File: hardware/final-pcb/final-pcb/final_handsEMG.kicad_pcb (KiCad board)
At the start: 2 copper layers, 192 parts, among them J1 Conn_02x13_Odd_Even, U1 ADS1299CPAG, U2 STM32L496ZGT6, U3 FT231XQ-R, U6 TPS60403DBVT, U8 TPS72325DBVT, U9 TPS73225DBVT

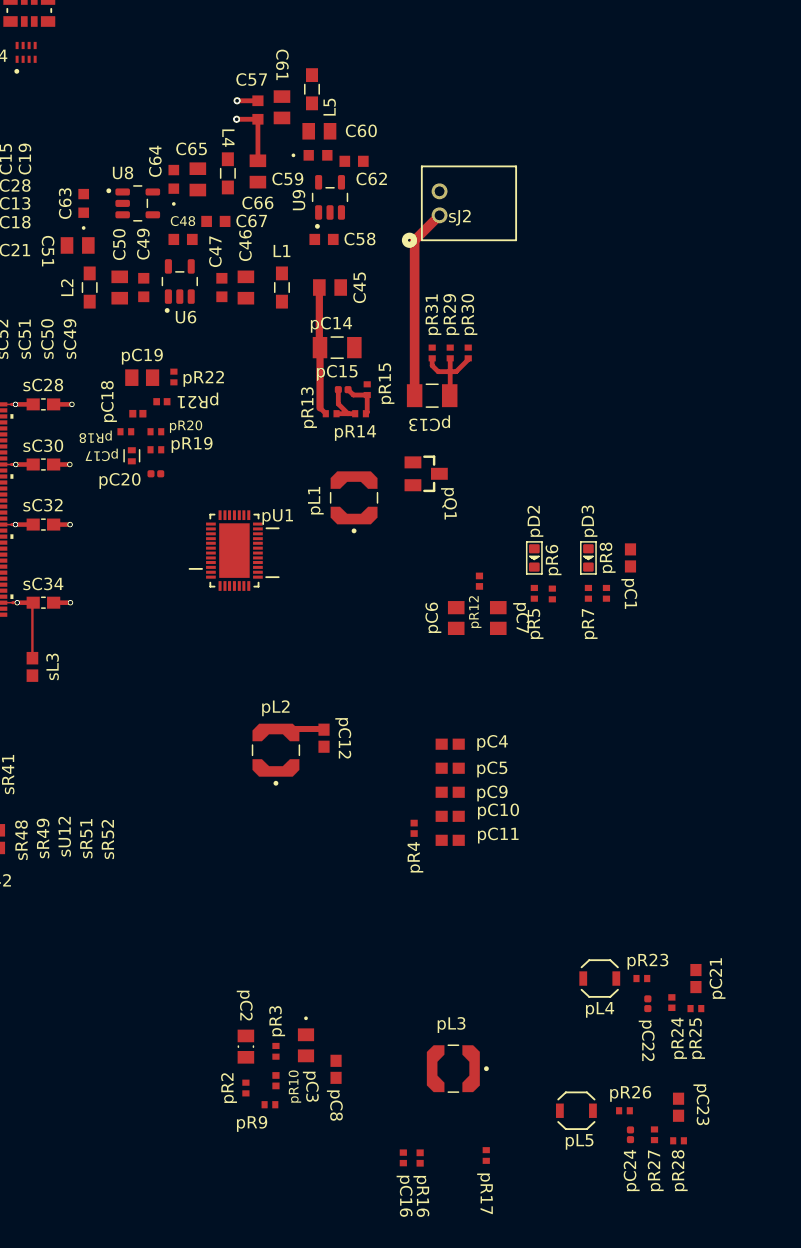
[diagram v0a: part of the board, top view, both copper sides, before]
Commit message: Power routed, not clean but in
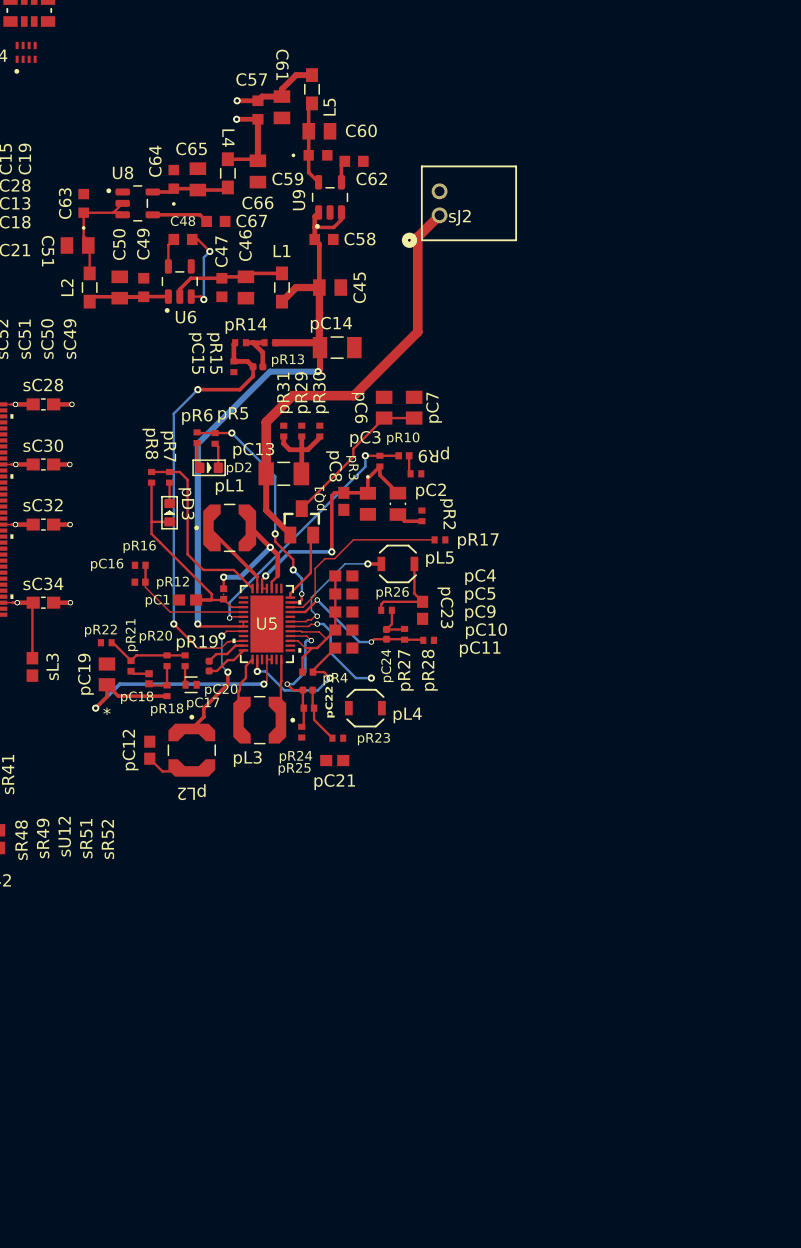
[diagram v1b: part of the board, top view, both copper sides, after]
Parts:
- removed pU1: LTC3586EUFE-3-PBF, 03PowerFOOTPRINTS:LTC3586EUFE
- added U5: LTC3586EUFE-3-PBF, footprints:QFN-38_UFE_LIT, F.Cu at (138.7, 99.5)
- pR34, pR35: value 1K -> 10K
- moved pC16 53.9 mm to (128.2, 94.6), turned to 180 degrees
- moved pR9 53.9 mm to (151.1, 87.0), turned to 180 degrees
- moved pR16 53.3 mm to (128.2, 96.0), turned to 180 degrees
- moved pR10 53.1 mm to (150.1, 85.5), turned to 180 degrees
- moved pR17 51.4 mm to (153.1, 92.5), turned to 0 degrees
- moved pR3 49.9 mm to (148.1, 85.9), turned to 90 degrees
- moved pR2 49.8 mm to (151.6, 90.5), turned to 90 degrees
- moved pL5 47.9 mm to (149.6, 94.5)
- moved pC8 47.3 mm to (145.1, 89.3)
- moved pC2 46.9 mm to (149.6, 89.5)
- moved pR27 46.5 mm to (150.2, 100.4)
- moved pR28 46.5 mm to (152.2, 100.9)
- moved pC23 46.5 mm to (151.7, 98.4)
- moved pC24 46.3 mm to (148.7, 100.4)
- moved pR26 46.1 mm to (148.7, 98.4)
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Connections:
- U1 pad 35: /PWDN -> PC4
- U1 pad 36: /RESET -> PC5
- U1 pad 38: START -> PB0
- U1 pad 39: /CS -> PA4
- U1 pad 40: SCLK -> PA1
- U1 pad 47: /DRDY -> PA5
- U2 pad 111: unconnected-(U2-PC10-Pad111) -> MODE
- U2 pad 112: unconnected-(U2-PC11-Pad112) -> ILIM1
- U2 pad 113: unconnected-(U2-PC12-Pad113) -> ILIM0
- U2 pad 114: unconnected-(U2-PD0-Pad114) -> *FAULT
- U2 pad 115: unconnected-(U2-PD1-Pad115) -> EN1
- U2 pad 116: unconnected-(U2-PD2-Pad116) -> EN2
- U2 pad 117: unconnected-(U2-PD3-Pad117) -> EN3
- U2 pad 118: unconnected-(U2-PD4-Pad118) -> EN4
- U2 pad 119: unconnected-(U2-PD5-Pad119) -> PD5
- U2 pad 122: unconnected-(U2-PD6-Pad122) -> PD6
- U2 pad 41: unconnected-(U2-PA5-Pad41) -> PA5
- U2 pad 42: PA6 -> DOUT
- U2 pad 43: PA7 -> DIN
- U2 pad 44: unconnected-(U2-PC4-Pad44) -> PC4
- U2 pad 45: unconnected-(U2-PC5-Pad45) -> PC5
- U2 pad 46: unconnected-(U2-PB0-Pad46) -> PB0
- dR6 pad 1: RXD -> PD5
- dR6 pad 2: Net-(U3-RXD) -> Net-(U4-RXD)
- dR7 pad 1: TXD -> PD6
- dR7 pad 2: Net-(U3-TXD) -> Net-(U4-TXD)
- pR34 pad 1: Net-(pJP7-Pad1) -> EN3
- pR35 pad 1: Net-(pJP8-Pad1) -> EN4
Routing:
- net 5VCC: track 10.7 -> 65.6 mm, vias 0 -> 2
- net PVIN3: track 4.02 -> 43.6 mm, vias 0 -> 2
- net FB4: track 3.38 -> 36.5 mm, vias 0 -> 2
- net AVOUT3: track 69.0 -> 94.1 mm, vias 19 -> 21
- net NTC: track 0.00 -> 22.1 mm, vias 0 -> 2
- net AVBUS: track 11.6 -> 32.9 mm, vias 0 -> 2
- net BAT: track 15.9 -> 36.8 mm
- net *CHRG: track 0.00 -> 20.2 mm, vias 0 -> 4
- net LDO3V3: track 0.00 -> 19.7 mm
- net -5VCC: track 0.00 -> 18.4 mm
- net *FAULT: track 0.00 -> 16.0 mm
- net PROG: track 0.00 -> 15.6 mm
- net unconnected-(U3-CTS#-Pad6): track 0.00 -> 13.2 mm, vias 0 -> 2
- net Net-(U3-RXD): track 13.2 -> 0.00 mm, vias 2 -> 0
- net FB1: track 0.00 -> 13.1 mm, vias 0 -> 2
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
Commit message: finalpcb is not final yet (4.12.25)
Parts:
- removed U5: LTC3586EUFE-3-PBF, footprints:QFN-38_UFE_LIT
- removed pC26, pC27: 0.1uF, 03PowerFOOTPRINTS:C1005X5R1C104K
- removed pJP2, pJP3, pJP4, pJP5, pJP6, pJP7, pJP8: TMM-103-02-L-S, 03PowerFOOTPRINTS:SAMTEC-TMM-103-02-X-S
- removed pR32, pR33: 1K, 03PowerFOOTPRINTS:CRCW04021K00JNED
- added U3: LTC3586EUFE-3-PBF, 03PowerFOOTPRINTS:LTC3586EUFE, F.Cu at (145.7, 99.9)
- moved pR34 54.4 mm to (177.9, 47.7)
- moved pR35 54.4 mm to (177.9, 49.9)
- moved pC29 47.1 mm to (177.9, 45.5)
- moved pC28 41.4 mm to (177.9, 43.4)
- moved pD3 30.2 mm to (156.7, 74.8), turned to -90 degrees
- moved pR9 28.2 mm to (131.8, 107.5), turned to 0 degrees
- moved pR10 27.6 mm to (131.8, 106.1)
- moved pC19 27.2 mm to (151.2, 112.4), turned to -90 degrees
- moved C63 26.0 mm to (147.0, 53.5), turned to 0 degrees
- moved pR15 25.5 mm to (140.7, 103.1), turned to 0 degrees
- moved C51 24.6 mm to (147.5, 70.1), turned to 90 degrees
- moved pR3 24.5 mm to (131.8, 104.2), turned to 180 degrees
- moved pR14 23.7 mm to (140.2, 99.5), turned to 180 degrees
- moved pC15 23.5 mm to (140.7, 101.4), turned to 0 degrees
- moved U8 23.1 mm to (145.3, 49.2), turned to 90 degrees
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- renumbered U3 to U4
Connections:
- U2 pad 107: GND -> DGND
- U2 pad 120: GND -> DGND
- U2 pad 130: GND -> DGND
- U2 pad 143: GND -> DGND
- U2 pad 16: GND -> DGND
- U2 pad 30: GNDA -> DGND
- U2 pad 31: GNDA -> DGND
- U2 pad 38: GND -> DGND
- U2 pad 51: GND -> DGND
- U2 pad 6: VBAT -> AVOUT3
- U2 pad 61: GND -> DGND
- U2 pad 71: GND -> DGND
- U2 pad 83: GND -> DGND
- U2 pad 94: GND -> DGND
- U4 pad 1: Net-(U3-RXD) -> Net-(U4-RXD)
- U4 pad 12: AVBUS -> AVOUT3
- U4 pad 13: GND -> DGND
- U4 pad 17: Net-(U3-TXD) -> Net-(U4-TXD)
- U4 pad 18: DTR# -> unconnected-(U4-DTR#-Pad18)
- U4 pad 20: 3V3OUT -> AVOUT3
- U4 pad 21: GND -> DGND
- U4 pad 3: GND -> DGND
- dC1 pad 2: GND -> DGND
- dC2 pad 2: GND -> DGND
- dC3 pad 2: GND -> DGND
- dD3 pad 2: GND -> DGND
- pC1 pad 2: GND -> DGND
- pC10 pad 2: GND -> DGND
- pC11 pad 2: GND -> DGND
- pC12 pad 2: GND -> DGND
- pC14 pad 2: GND -> DGND
- pC16 pad 2: GND -> DGND
- pC19 pad 2: GND -> DGND
- pC21 pad 1: GND -> DGND
- pC23 pad 1: GND -> DGND
- pC28 pad 2: GND -> DGND
- pC29 pad 2: GND -> DGND
- pC3 pad 2: GND -> DGND
- pC4 pad 2: GND -> DGND
- pC5 pad 2: GND -> DGND
- pC6 pad 2: GND -> DGND
- pC7 pad 2: GND -> DGND
- pC8 pad 2: GND -> DGND
- pC9 pad 2: GND -> DGND
- pR15 pad 1: GND -> DGND
- pR16 pad 2: GND -> DGND
- pR17 pad 2: GND -> DGND
- pR2 pad 2: GND -> DGND
- pR22 pad 2: GND -> DGND
- pR25 pad 2: GND -> DGND
- pR28 pad 2: GND -> DGND
- pR29 pad 1: GND -> DGND
- pR30 pad 1: GND -> DGND
- pR31 pad 1: GND -> DGND
- pR9 pad 1: GND -> DGND
- sC28 pad 2: GND -> DGND
- sC29 pad 2: GND -> DGND
- sC30 pad 2: GND -> DGND
- sC31 pad 2: GND -> DGND
- sC32 pad 2: GND -> DGND
- sC33 pad 2: GND -> DGND
- sC34 pad 2: GND -> DGND
- sC42 pad +: (no net) -> AVBUS
- sC42 pad -: (no net) -> DGND
- sC49 pad 2: GND -> DGND
- sC50 pad 2: GND -> DGND
- sC51 pad 2: GND -> DGND
- sC52 pad 2: GND -> DGND
- sC53 pad 2: GND -> DGND
- sC54 pad 2: GND -> DGND
- sC57 pad 2: GNDA -> DGND
- sC58 pad 2: GNDA -> DGND
- sC60 pad 2: GND -> DGND
- sC61 pad 2: GND -> DGND
- sCN14 pad 5: GND -> DGND
- sD10 pad 2: GND -> DGND
- sD6 pad 2: GND -> DGND
- sJ2 pad 2: GND -> DGND
- sJ3 pad 5: GND -> DGND
- sJ3 pad 7: GND -> DGND
- sLD7 pad +: (no net) -> Net-(sLD7-A)
- sLD7 pad -: (no net) -> Net-(sLD7-K)
- sLD8 pad +: (no net) -> Net-(sLD8-A)
- sLD8 pad -: (no net) -> Net-(sLD8-K)
- sR38 pad 2: GND -> DGND
- sR48 pad 1: GND -> DGND
- sR52 pad 2: GND -> DGND
- sT2 pad 2: GND -> DGND
- sU12 pad 2: GND -> DGND
- sU13 pad 2: GND -> DGND
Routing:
- net AVSS: track 7.78 -> 151.8 mm, vias 1 -> 20
- net AVDD: track 13.4 -> 149.9 mm, vias 3 -> 17
- net DGND: track 0.00 -> 129.9 mm, vias 0 -> 73
- net AVBUS: track 32.9 -> 122.8 mm, vias 2 -> 6
- net GNDA: track 2.88 -> 82.3 mm, vias 2 -> 52
- net ILIM1: track 0.00 -> 78.9 mm, vias 0 -> 2
- net ILIM0: track 0.00 -> 78.0 mm, vias 0 -> 2
- net EN2: track 0.00 -> 76.8 mm, vias 0 -> 3
- net EN1: track 0.00 -> 74.1 mm, vias 0 -> 2
- net EN4: track 0.00 -> 67.4 mm, vias 0 -> 2
- net MODE: track 0.00 -> 67.0 mm, vias 0 -> 2
- net EN3: track 0.00 -> 66.7 mm, vias 0 -> 2
- net *FAULT: track 16.0 -> 77.4 mm, vias 0 -> 3
- net PA10: track 0.00 -> 52.5 mm, vias 0 -> 2
- net PA5: track 0.00 -> 46.9 mm, vias 0 -> 2
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- added copper zone on In1.Cu, net AVDD
- added copper zone on In1.Cu, net AVOUT3
- added copper zone on B.Cu, net DGND
- added copper zone on F.Cu, net DGND
- added copper zone on In2.Cu, net DGND
- added copper zone on B.Cu, net GNDA
- added copper zone on F.Cu, net GNDA
- added copper zone on In2.Cu, net GNDA
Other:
- board outline added: 85.2 x 104 mm
- copper layers 2 -> 4

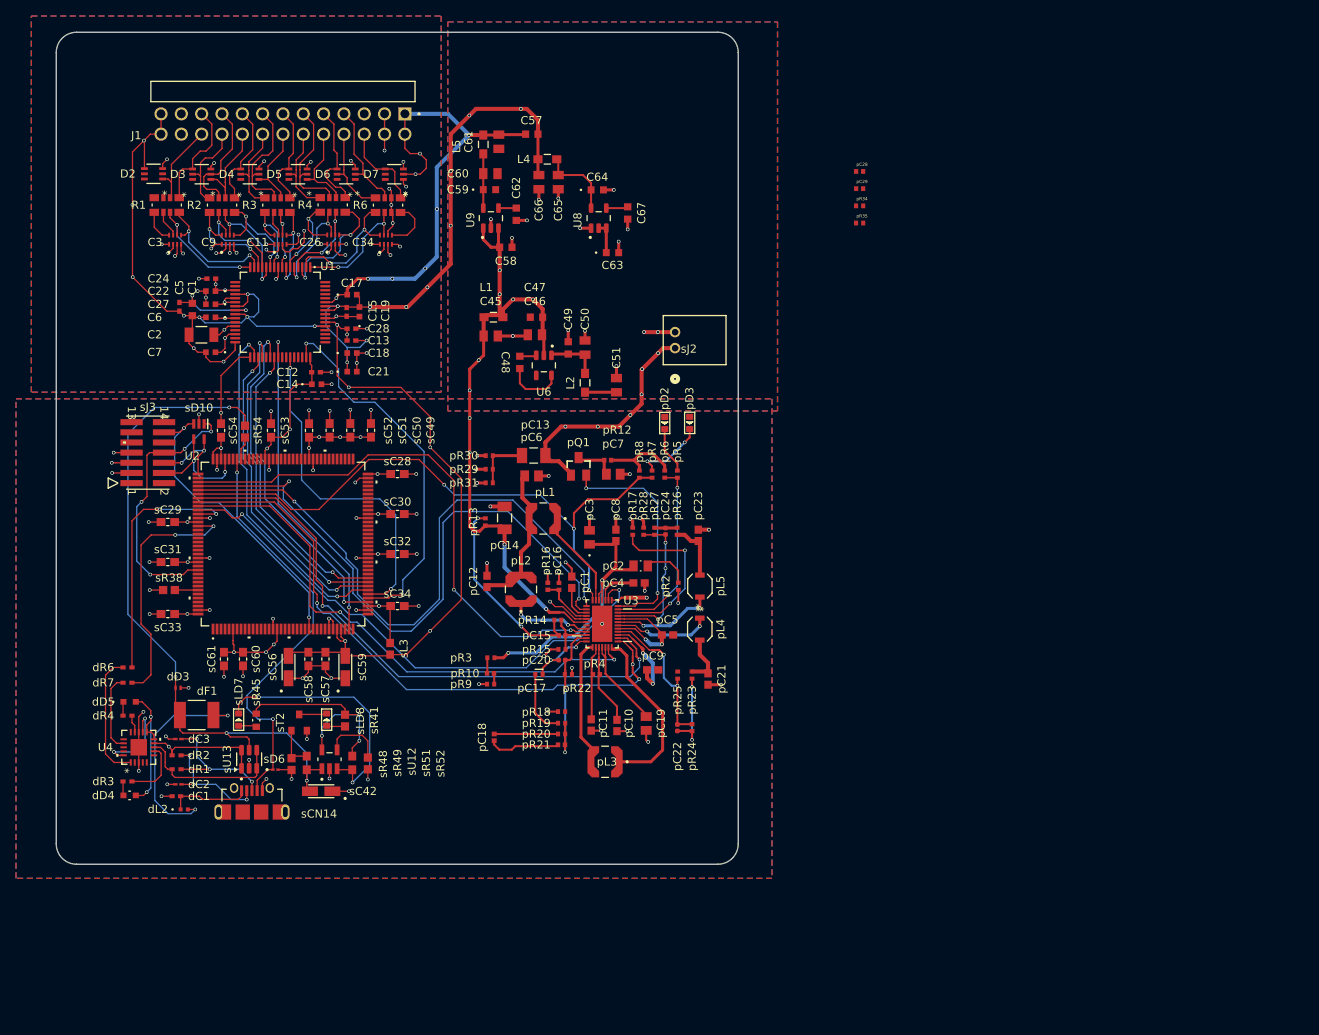
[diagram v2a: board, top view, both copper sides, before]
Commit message: traces got fucked up so i rerouted pmic (4.13.25)
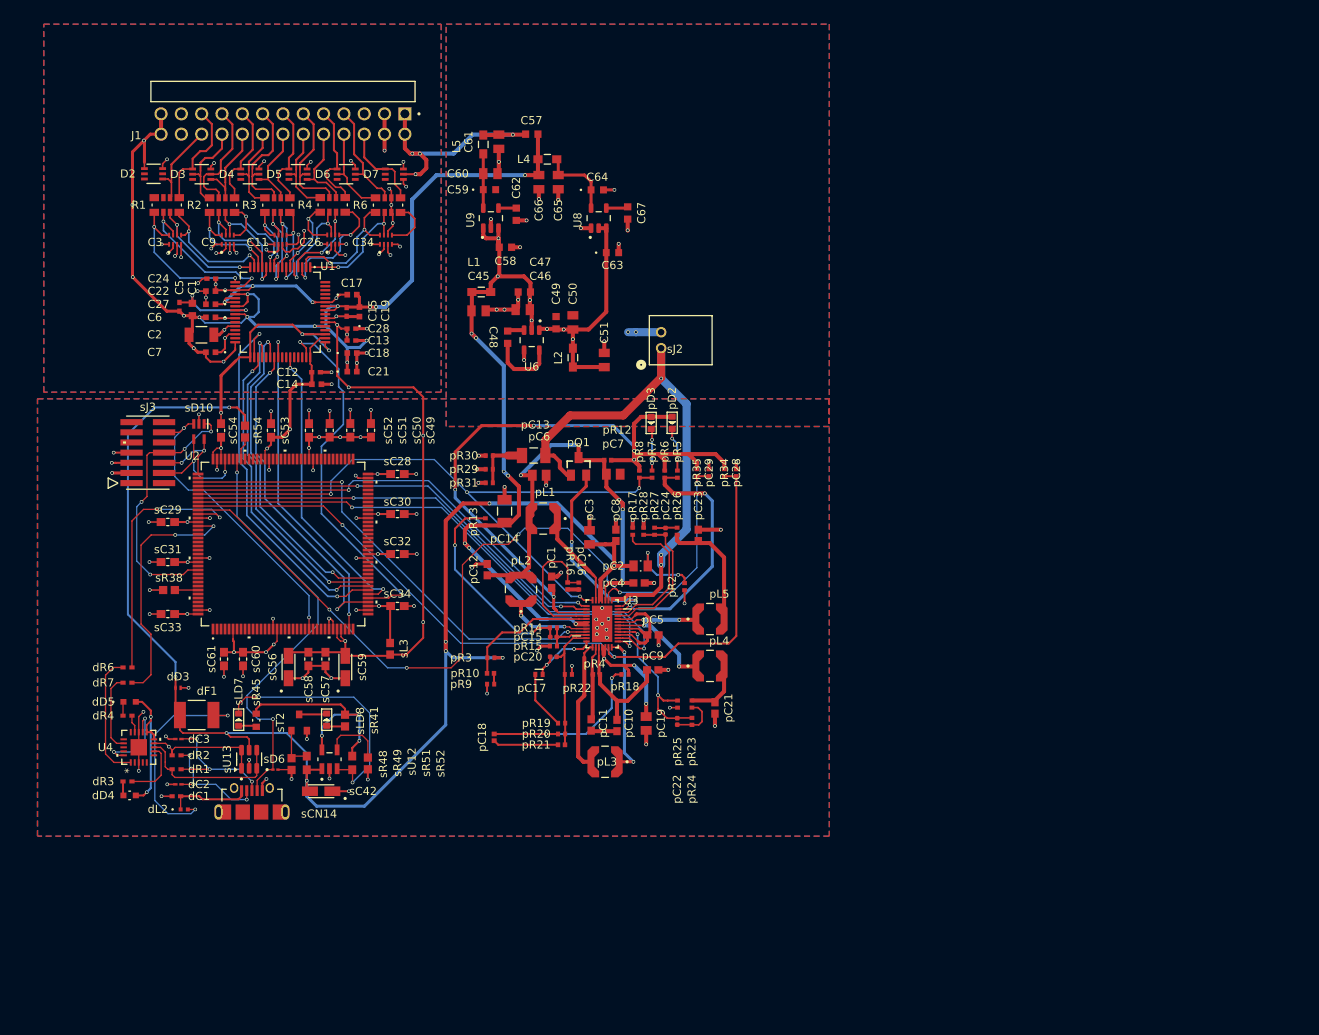
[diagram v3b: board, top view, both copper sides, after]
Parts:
- pL4, pL5: footprint 03PowerFOOTPRINTS:IND_3010_TDK -> LPS4018_472MRC:IND_LPS4018-472MRC
- moved pC28 40.7 mm to (162.5, 81.1), turned to 90 degrees
- moved pC29 40.2 mm to (159.1, 81.1), turned to 90 degrees
- moved pR34 37.4 mm to (161.0, 81.1), turned to 90 degrees
- moved pR35 37.3 mm to (157.6, 81.1), turned to 90 degrees
- moved pR18 9.19 mm to (148.6, 106.3)
- moved pD3 4.81 mm to (151.9, 74.8)
- moved pL4 4.77 mm to (159.2, 105.2), turned to 0 degrees
- moved pL5 4.31 mm to (159.2, 99.4), turned to 0 degrees
- moved pC21 3.72 mm to (159.8, 110.5)
- moved pR23 3.62 mm to (157.0, 110.0)
- moved pR25 3.62 mm to (155.2, 110.0), turned to -90 degrees
- moved C51 3.50 mm to (146.0, 67.0)
- moved C47 3.50 mm to (136.0, 58.5)
- moved C49 3.50 mm to (140.0, 62.3)
- moved L1 3.50 mm to (130.6, 58.5)
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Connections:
- C45 pad 2: GNDA -> DGND
- C46 pad 2: GNDA -> DGND
- C47 pad 2: GNDA -> DGND
- C49 pad 2: GNDA -> DGND
- C50 pad 2: GNDA -> DGND
- C51 pad 2: GNDA -> DGND
- C58 pad 2: GNDA -> DGND
- C59 pad 2: GNDA -> DGND
- C60 pad 2: GNDA -> DGND
- C61 pad 2: GNDA -> DGND
- C62 pad 2: GNDA -> DGND
- C63 pad 2: GNDA -> DGND
- C64 pad 2: GNDA -> DGND
- C65 pad 2: GNDA -> DGND
- C66 pad 2: GNDA -> DGND
- C67 pad 2: GNDA -> DGND
- U6 pad 4: GNDA -> DGND
- U8 pad 1: GNDA -> DGND
- U9 pad 2: GNDA -> DGND
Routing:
- net LDO3V3: track 13.5 -> 88.0 mm, vias 0 -> 5
- net AVBUS: track 122.8 -> 184.8 mm, vias 6 -> 9
- net DGND: track 129.9 -> 174.7 mm, vias 73 -> 98
- net EN4: track 67.4 -> 106.3 mm, vias 2 -> 5
- net BAT: track 34.1 -> 68.3 mm, vias 7 -> 3
- net EN3: track 66.7 -> 98.6 mm
- net ILIM1: track 78.9 -> 53.6 mm
- net PVIN3: track 60.3 -> 81.3 mm, vias 4 -> 5
- net ILIM0: track 78.0 -> 57.0 mm
- net GNDA: track 82.3 -> 63.6 mm, vias 52 -> 39
- net SRB2: track 3.35 -> 20.5 mm, vias 0 -> 2
- net SRB1: track 4.13 -> 19.3 mm, vias 0 -> 2
- net -5VCC: track 14.6 -> 29.4 mm, vias 0 -> 3
- net AVDD: track 149.9 -> 135.8 mm, vias 17 -> 16
- net Net-(pC18-Pad1): track 9.21 -> 22.7 mm, vias 1 -> 2
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- added copper zone on In1.Cu, net AVSS
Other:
- board outline removed

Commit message: basically done, everyone please verify if possible (4.16.25)
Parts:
- added C16: 1nF, CC0402KRX7R7BB102:YAG_CC0402_YAG, F.Cu at (114.4, 57.4)
- added G***: LOGO, LOGO, F.Cu at (156.9, 49.1)
- added R5: 1M, RC0402JR-071ML:RC0402N_YAG, F.Cu at (114.4, 56.0)
- added REF**: MountingHole_2.1mm, MountingHole:MountingHole_2.1mm, F.Cu at (82.5, 34.6)
- added REF**: MountingHole_2.1mm, MountingHole:MountingHole_2.1mm, F.Cu at (163.3, 123.9)
- added REF**: MountingHole_2.1mm, MountingHole:MountingHole_2.1mm, F.Cu at (163.3, 34.6)
- added REF**: MountingHole_2.1mm, MountingHole:MountingHole_2.1mm, F.Cu at (82.5, 123.9)
- added TP1: RAW, 5000:KEYSTONE_5000, F.Cu at (161.6, 73.6)
- added TP2: LDO3V3, 5000:KEYSTONE_5000, F.Cu at (137.2, 72.0)
- added TP4: +3V3, 5000:KEYSTONE_5000, F.Cu at (146.0, 121.7)
- added TP5: -5V, 5001:KEYSTONE_5001, F.Cu at (150.8, 58.5)
- added TP6: +5V, 5001:KEYSTONE_5001, F.Cu at (129.4, 67.6)
- added TP7: +2V5, 5001:KEYSTONE_5001, F.Cu at (129.6, 35.8)
- added TP8: -2V5, 5001:KEYSTONE_5001, F.Cu at (145.2, 38.8)
- moved BAT 4.65 mm to (157.8, 65.5)
- moved SWD 2.47 mm to (86.5, 78.5)
- renumbered sJ2 to BAT, sJ3 to SWD
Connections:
- C3 pad 7: SRB2 -> _SRB2
- C3 pad 8: SRB1 -> _SRB1
- R1 pad 5: SRB1 -> _SRB1
- R1 pad 6: SRB2 -> _SRB2
- U1 pad 17: SRB1 -> _SRB1
- U1 pad 18: SRB2 -> _SRB2
- U1 pad 63: BIASOUT -> BIASIN
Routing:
- net _SRB2: track 0.00 -> 20.5 mm, vias 0 -> 2
- net _SRB1: track 0.00 -> 19.3 mm, vias 0 -> 2
- net AVOUT3: track 126.8 -> 144.7 mm
- net BIAS_DRV: track 6.45 -> 19.8 mm
- net BAT: track 68.3 -> 80.6 mm, vias 3 -> 5
- net AVSS: track 143.3 -> 151.4 mm
- net SRB2: track 20.5 -> 13.6 mm, vias 2 -> 1
- net BIASIN: track 0.00 -> 6.79 mm
- net -5VCC: track 29.4 -> 35.9 mm, vias 3 -> 1
- net SRB1: track 19.3 -> 13.0 mm, vias 2 -> 0
- net AVDD: track 135.8 -> 142.0 mm, vias 16 -> 11
- net 5VCC: track 84.2 -> 89.4 mm, vias 11 -> 7
- net LDO3V3: track 88.0 -> 91.1 mm
- net PA13: track 14.7 -> 17.2 mm
- net PA14: track 10.3 -> 12.8 mm
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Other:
- board outline added: 85.9 x 94.4 mm
- board text added: "1N 1P"
- board text added: "2N 2P"
- board text added: "3N 3P"
- board text added: "4N 4P"
- board text added: "5N 5P"
- board text added: "6N 6P"
- board text added: "7N 7P"
- board text added: "8N 8P"
- board text added: "AVDD AVDD"
- board text added: "AVSS AVSS"
- board text added: "BIAS BIAS"
- board text added: "Computer Engineer(s): Blake Pearson Noah Marosok"
- board text added: "Electrical Engineer(s): Jayden Sumbillo Kelly Hubbard Kirk Young"
- board text added: "GNDA GNDA"
- board text added: "NRST"
- board text added: "PB3 PA14 PA13"
- board text added: "SRB2 SRB1"
- board text added: "Team HANDS-EMG"
